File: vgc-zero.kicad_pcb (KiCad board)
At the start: 2 copper layers, 53 x 82 mm, 22 parts, among them J1 Conn_01x05_Pin, J2 Conn_01x05_Pin, J3 Conn_01x05_Pin, J4 Conn_01x02_Pin, SW1 SW_Push, SW10 SW_Push, SW11 SW_SPDT, SW2 SW_Push, SW3 SW_Push, SW4 SW_Push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

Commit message: pcb done
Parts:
- removed J4: Conn_01x02_Pin, Connector_PinHeader_1.00mm:PinHeader_1x02_P1.00mm_Horizontal
- added ?: , , F.Cu at (77.5, 79.5)
- added ?: , , F.Cu at (77.5, 75.0)
- added ?: , , F.Cu at (72.5, 79.0)
- added ?: , , F.Cu at (75.5, 73.0)
- added ?: , , F.Cu at (79.0, 82.0)
- added ?: , , F.Cu at (82.5, 75.5)
- added ?: , , F.Cu at (79.5, 73.0)
- added ?: , , F.Cu at (75.5, 82.0)
- added ?: , , F.Cu at (72.5, 75.5)
- added ?: , , F.Cu at (82.5, 79.0)
- added ?: , , F.Cu at (75.5, 77.0)
- added ?: , , F.Cu at (79.5, 77.0)
- added H1: MountingHole_Pad, MountingHole:MountingHole_3.2mm_M3_Pad, F.Cu at (77.0, 90.5)
- added REF**: MountingHole_2.2mm_M2, MountingHole:MountingHole_2.2mm_M2, F.Cu at (100.5, 40.5)
- D1: footprint LED_THT:LED_D3.0mm -> LED_SMD:LED_1210_3225Metric_Pad1.42x2.65mm_HandSolder
- J1, J2, J3: value Conn_01x05_Pin -> Conn_01x06_Pin; footprint Connector_PinHeader_1.00mm:PinHeader_1x05_P1.00mm_Horizontal -> Connector_PinHeader_2.54mm:PinHeader_1x06_P2.54mm_Horizontal
- moved J3 17.5 mm to (53.6, 114.6)
- moved J1 7.14 mm to (70.2, 114.6)
- moved D1 5.52 mm to (99.0, 46.0), turned to 0 degrees
- moved J2 4.17 mm to (86.7, 114.6)
- moved CHARGER1 1.03 mm to (75.0, 54.8)
- moved LS1 1.00 mm to (79.3, 68.5)
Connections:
- DISP1 pad 2: /3V3 -> 3V3
- MCU1 pad 36: /3V3 -> 3V3
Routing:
- net 3V3: track 0.00 -> 149.8 mm, vias 0 -> 2
- net /3V3: track 109.9 -> 0.00 mm, vias 3 -> 0
- net Net-(MCU1-GPIO7): track 31.5 -> 43.7 mm
- net Net-(MCU1-GPIO6): track 30.0 -> 38.6 mm
- net Net-(MCU1-GPIO9): track 24.4 -> 32.8 mm
- net Net-(J3-Pin_5): track 61.0 -> 52.9 mm
- net Net-(MCU1-GPIO10): track 39.3 -> 47.3 mm
- net Net-(MCU1-GPIO2): track 14.6 -> 22.6 mm
- net Net-(MCU1-GPIO5): track 37.2 -> 45.2 mm
- net Net-(MCU1-GPIO4): track 28.5 -> 36.5 mm
- net Net-(MCU1-GPIO3): track 39.3 -> 47.3 mm
- net Net-(MCU1-GPIO8): track 46.5 -> 54.5 mm
- net Net-(MCU1-GPIO11): track 11.0 -> 19.0 mm
- net Net-(J2-Pin_4): track 61.2 -> 53.5 mm
- net Net-(J2-Pin_5): track 59.2 -> 51.4 mm
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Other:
- board size 53 x 82 mm -> 53 x 87.5 mm
- board text added: "330Ω"

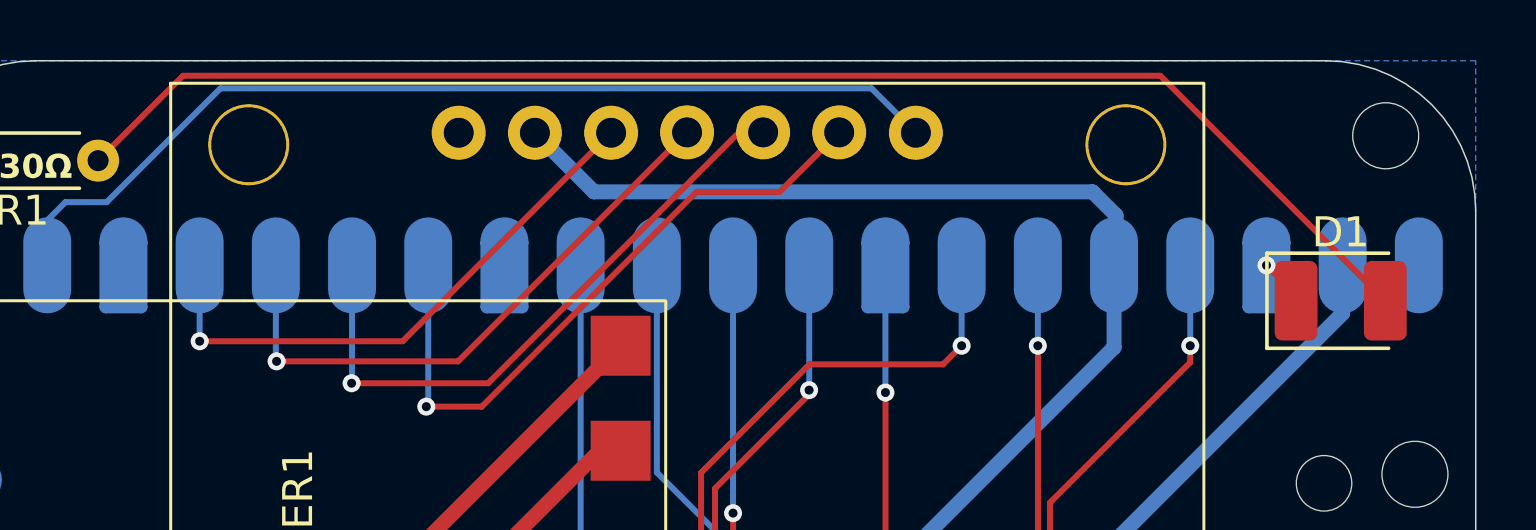
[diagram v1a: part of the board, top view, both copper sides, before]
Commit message: move via off the pad
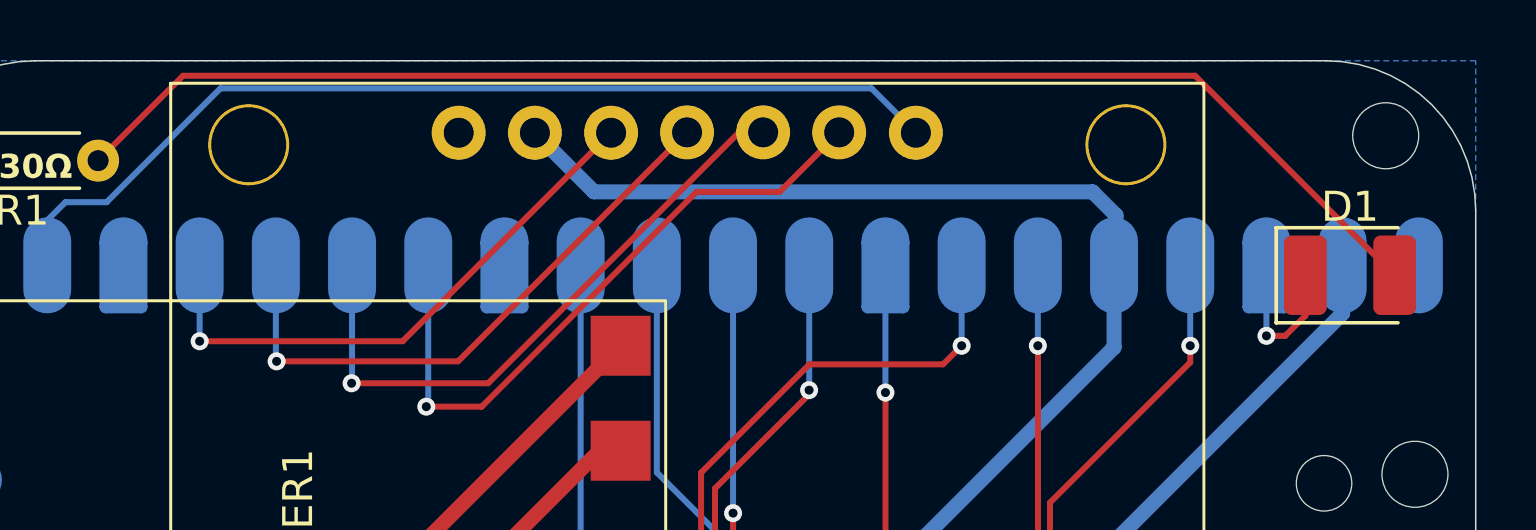
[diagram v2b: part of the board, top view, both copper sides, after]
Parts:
- moved D1 0.90 mm to (99.3, 45.1)
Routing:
- net /GND: track 16.8 -> 20.7 mm
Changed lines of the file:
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@@
 	(footprint "LED_SMD:LED_1210_3225Metric_Pad1.42x2.65mm_HandSolder"
 		(layer "F.Cu")
-		(at 99 46)
+		(at 99.31 45.15)
 		(descr "LED SMD 1210 (3225 Metric), square (rectangular) end terminal, IPC-7351 nominal, (Body size source: http://www.tortai-tech.com/upload/download/2011102023233369053.pdf), generated with kicad-footprint-generator")
 		(tags "LED handsolder")
@@
 	)
 	(segment
-		(start 97.5125 45.8075)
-		(end 96.525 44.82)
+		(start 97.15 47.17)
+		(end 97.8225 46.4975)
 		(width 0.2)
 		(layer "F.Cu")
@@
 	)
 	(segment
+		(start 97.8225 46.4975)
+		(end 97.8225 45.15)
+		(width 0.2)
+		(layer "F.Cu")
+		(net 3)
+	)
+	(segment
+		(start 96.525 47.17)
+		(end 97.15 47.17)
+		(width 0.2)
+		(layer "F.Cu")
+		(net 3)
+	)
+	(segment
 		(start 97.5125 46)
 		(end 97.5125 45.8075)
@@
 	)
 	(via
-		(at 96.525 44.82)
+		(at 96.525 47.17)
 		(size 0.6)
 		(drill 0.3)
@@
 	)
 	(segment
+		(start 96.525 47.17)
+		(end 96.525 44.82)
+		(width 0.2)
+		(layer "B.Cu")
+		(net 3)
+	)
+	(segment
 		(start 71.125 64.2)
 		(end 71.125 62.375)
@@
 	)
 	(segment
-		(start 100.4875 46)
-		(end 92.9875 38.5)
+		(start 100.7975 45.15)
+		(end 94.1475 38.5)
 		(width 0.2)
 		(layer "F.Cu")
@@
 	)
 	(segment
-		(start 92.9875 38.5)
+		(start 94.1475 38.5)
 		(end 60.41 38.5)
 		(width 0.2)

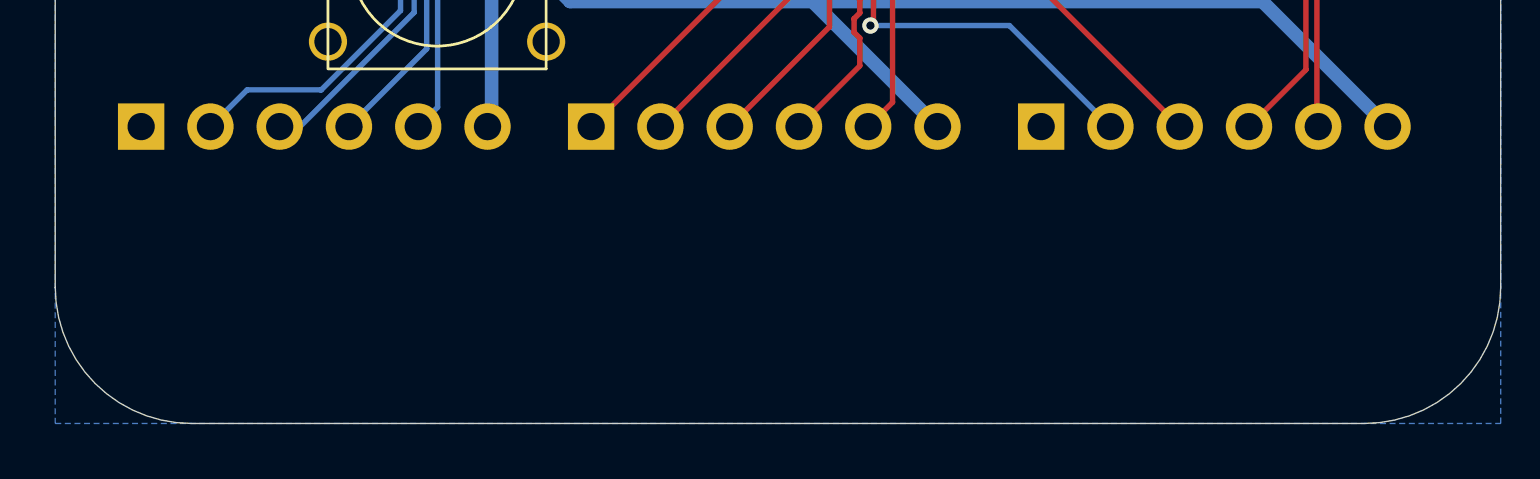
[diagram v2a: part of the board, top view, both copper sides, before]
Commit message: add markings
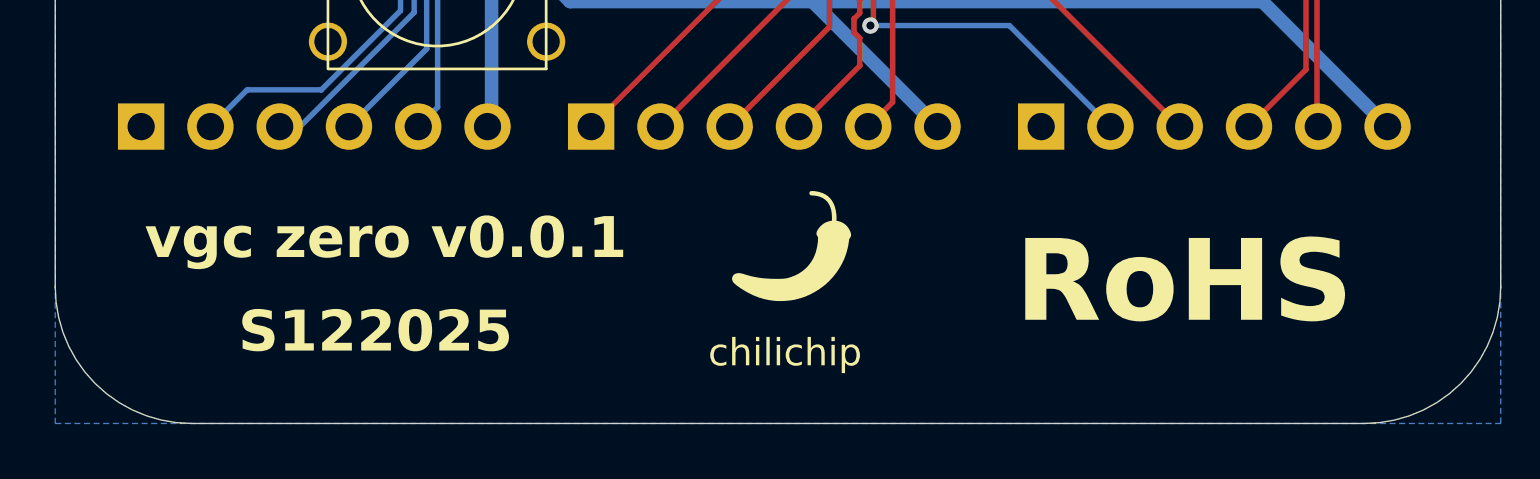
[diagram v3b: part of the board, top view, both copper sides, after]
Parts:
- added G***: LOGO, LOGO, F.Cu at (77.5, 119.1)
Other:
- board text added: "RoHS"
- board text added: "S122025"
- board text added: "chilichip"
- board text added: "vgc zero v0.0.1"

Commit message: final touches
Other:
- board text added: "vgc zero v0.0.2"
- board text removed: "vgc zero v0.0.1"
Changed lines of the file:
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@@
 	)
 	(paper "A4")
+	(title_block
+		(title "vgc zero")
+		(rev "v0.0.2")
+		(comment 4 "Author: Kacper Akdag-Ochnik")
+	)
 	(layers
 		(0 "F.Cu" signal)
@@
 		(tenting front back)
 		(pcbplotparams
-			(layerselection 0x00000000_00000000_55555555_5755f5ff)
+			(layerselection 0x00000000_00000000_55555555_575555ff)
 			(plot_on_all_layers_selection 0x00000000_00000000_00000000_00000000)
 			(disableapertmacros no)
@@
 			(usegerberattributes yes)
 			(usegerberadvancedattributes yes)
-			(creategerberjobfile yes)
+			(creategerberjobfile no)
 			(dashed_line_dash_ratio 12.000000)
 			(dashed_line_gap_ratio 3.000000)
@@
 			(outputformat 1)
 			(mirror no)
-			(drillshape 1)
+			(drillshape 0)
 			(scaleselection 1)
-			(outputdirectory "")
+			(outputdirectory "gerbers/")
 		)
 	)
@@
 		(layer "Edge.Cuts")
 	)
-	(gr_text "vgc zero v0.0.1"
+	(gr_text "vgc zero v0.0.2"
 		(at 53.78 119.58 0)
 		(layer "F.SilkS")
@@
 		)
 	)
+	(dimension
+		(type orthogonal)
+		(layer "F.SilkS")
+		(pts
+			(xy 103.5 120.5) (xy 50.5 120.5)
+		)
+		(height 8.55)
+		(orientation 0)
+		(format
+			(prefix "")
+			(suffix "")
+			(units 3)
+			(units_format 0)
+			(precision 4)
+			(suppress_zeroes yes)
+		)
+		(style
+			(thickness 0.1)
+			(arrow_length 1.27)
+			(text_position_mode 0)
+			(arrow_direction outward)
+			(extension_height 0.58642)
+			(extension_offset 0.5)
+			(keep_text_aligned yes)
+		)
+		(gr_text "53"
+			(at 77 127.95 0)
+			(layer "F.SilkS")
+			(effects
+				(font
+					(size 1 1)
+					(thickness 0.1)
+				)
+			)
+		)
+	)
+	(dimension
+		(type orthogonal)
+		(layer "F.SilkS")
+		(pts
+			(xy 98.5 38) (xy 98.5 125.5)
+		)
+		(height 8.97)
+		(orientation 1)
+		(format
+			(prefix "")
+			(suffix "")
+			(units 3)
+			(units_format 0)
+			(precision 4)
+			(suppress_zeroes yes)
+		)
+		(style
+			(thickness 0.1)
+			(arrow_length 1.27)
+			(text_position_mode 0)
+			(arrow_direction outward)
+			(extension_height 0.58642)
+			(extension_offset 0.5)
+			(keep_text_aligned yes)
+		)
+		(gr_text "87.5"
+			(at 106.37 81.75 90)
+			(layer "F.SilkS")
+			(effects
+				(font
+					(size 1 1)
+					(thickness 0.1)
+				)
+			)
+		)
+	)

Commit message: bump all the way to 1.0.0
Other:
- board text removed: "330Ω"
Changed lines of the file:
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@@
 	(title_block
 		(title "vgc zero")
-		(rev "v0.0.2")
+		(rev "v1.0.0")
+		(comment 3 "Company: chilichip")
 		(comment 4 "Author: Kacper Akdag-Ochnik")
 	)
@@
 				(bold yes)
 			)
-			(justify left bottom)
-		)
-	)
-	(gr_text "330Ω"
-		(at 53.5 42 0)
-		(layer "F.SilkS")
-		(effects
-			(font
-				(size 0.8 0.8)
-				(thickness 0.1)
-				(bold yes)
-			)

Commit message: minor fixes
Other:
- board text added: "vgc zero v1.0.1"
- board text removed: "vgc zero v0.0.2"
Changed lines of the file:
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@@
 	(title_block
 		(title "vgc zero")
-		(rev "v1.0.0")
+		(rev "v1.0.1")
 		(comment 3 "Company: chilichip")
 		(comment 4 "Author: Kacper Akdag-Ochnik")
@@
 		(at 69.6 40.4)
 		(property "Reference" "DISP1"
-			(at 7.62 17.85 0)
+			(at 22.08 37.36 0)
 			(unlocked yes)
 			(layer "F.SilkS")
@@
 		(layer "Edge.Cuts")
 	)
-	(gr_text "vgc zero v0.0.2"
+	(gr_text "vgc zero v1.0.1"
 		(at 53.78 119.58 0)
 		(layer "F.SilkS")

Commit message: update to 1.1.0
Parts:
- removed ? (x12): , 
- removed BT1: LIPO-BATTERY, Connector_JST:JST_PH_S2B-PH-K_1x02_P2.00mm_Horizontal
- removed CHARGER1: TP4056_CHARGER, vgc-zero-footprints:Tp4056_Charger
- removed REF**: MountingHole_2.2mm_M2, MountingHole:MountingHole_2.2mm_M2
- added H2: MountingHole_Pad, MountingHole:MountingHole_2.2mm_M2_Pad, F.Cu at (99.2, 44.0)
- added H3: MountingHole_Pad, MountingHole:MountingHole_2.2mm_M2_Pad, F.Cu at (59.8, 76.0)
- added H4: MountingHole_Pad, MountingHole:MountingHole_2.2mm_M2_Pad, F.Cu at (99.2, 76.0)
- added H5: MountingHole_Pad, MountingHole:MountingHole_2.2mm_M2_Pad, F.Cu at (59.8, 111.8)
- added H6: MountingHole_Pad, MountingHole:MountingHole_2.2mm_M2_Pad, F.Cu at (99.2, 111.8)
- DISP1: footprint vgc-zero-footprints:SSD1351_OLED_128x128 -> Connector_JST:JST_PH_S7B-PH-K_1x07_P2.00mm_Horizontal; moved to B.Cu
- H1: footprint MountingHole:MountingHole_3.2mm_M3_Pad -> MountingHole:MountingHole_2.2mm_M2_Pad
- LS1: footprint Connector_Wire:SolderWire-0.1sqmm_1x02_P3.6mm_D0.4mm_OD1mm -> Buzzer_Beeper:Buzzer_12x9.5RM7.6
- MCU1: footprint Module:RaspberryPi_Pico_SMD_HandSolder -> Module:RaspberryPi_Pico_Common_THT
- SW1, SW10, SW2, SW3, SW4, SW5, SW6, SW7, SW8, SW9: footprint vgc-zero-footprints:SW_PUSH_RUBBER_8mm -> Button_Switch_THT:SW_PUSH_6mm_H5mm
- moved H1 49.6 mm to (59.8, 44.0)
- moved J3 35.9 mm to (89.4, 117.5)
- moved DISP1 26.0 mm to (65.0, 66.0), turned to 90 degrees
- moved LS1 18.5 mm to (97.3, 64.0), turned to 90 degrees
- moved MCU1 18.5 mm to (88.4, 39.6), turned to 180 degrees
- moved SW10 14.8 mm to (62.5, 84.8), turned to 180 degrees
- moved J2 13.8 mm to (73.2, 117.5)
- moved J1 13.6 mm to (56.9, 117.5)
- moved SW2 12.4 mm to (103.0, 99.0), turned to -90 degrees
- moved SW1 12.2 mm to (103.0, 84.8), turned to 180 degrees
- moved SW4 10.3 mm to (93.5, 103.5), turned to -90 degrees
- moved SW11 9.88 mm to (57.2, 93.5)
- moved SW3 9.76 mm to (98.2, 89.0), turned to -90 degrees
- moved SW6 8.80 mm to (77.5, 98.4), turned to -90 degrees
- moved R1 7.83 mm to (60.2, 39.7)
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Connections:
- MCU1 pad 39: /VCC -> unconnected-(MCU1-VSYS-Pad39)
- SW11 pad 1: /VCC -> /GND
- SW11 pad 2: Net-(CHARGER1-OUT+) -> Net-(J2-Pin_3)
- SW11 pad 3: unconnected-(SW11-C-Pad3) -> 3V3
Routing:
- net /VCC: track 69.3 -> 0.00 mm, vias 1 -> 0
- net Net-(MCU1-GPIO16): track 3.84 -> 60.1 mm
- net Net-(CHARGER1-OUT+): track 45.5 -> 0.00 mm
- net Net-(J2-Pin_4): track 53.5 -> 94.5 mm, vias 1 -> 0
- net Net-(MCU1-GPIO11): track 19.0 -> 51.2 mm
- net Net-(J2-Pin_3): track 80.9 -> 112.4 mm, vias 1 -> 0
- net Net-(J3-Pin_2): track 59.0 -> 31.1 mm
- net Net-(J2-Pin_5): track 51.4 -> 79.2 mm, vias 1 -> 0
- net Net-(BT1--): track 27.0 -> 0.00 mm
- net Net-(BT1-+): track 24.2 -> 0.00 mm
- net Net-(J2-Pin_2): track 79.5 -> 56.2 mm, vias 2 -> 0
- net Net-(J3-Pin_3): track 56.1 -> 34.7 mm
- net Net-(MCU1-GPIO2): track 22.6 -> 42.9 mm
- net Net-(MCU1-GPIO9): track 32.8 -> 50.4 mm
- net Net-(J1-Pin_3): track 78.8 -> 61.3 mm, vias 1 -> 0
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- added copper zone on F.Cu, net /GND
- removed copper zone on B.Cu, net /GND
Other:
- board size 53 x 87.5 mm -> 50 x 90 mm
- board text added: "A"
- board text added: "B"
- board text added: "S012026"
- board text added: "X"
- board text added: "Y"
- board text added: "vgc zero v1.1.0"
- board text added: "≣"
- board text added: "⌂"
- board text added: "△"
- board text removed: "S122025"
- board text removed: "vgc zero v1.0.1"

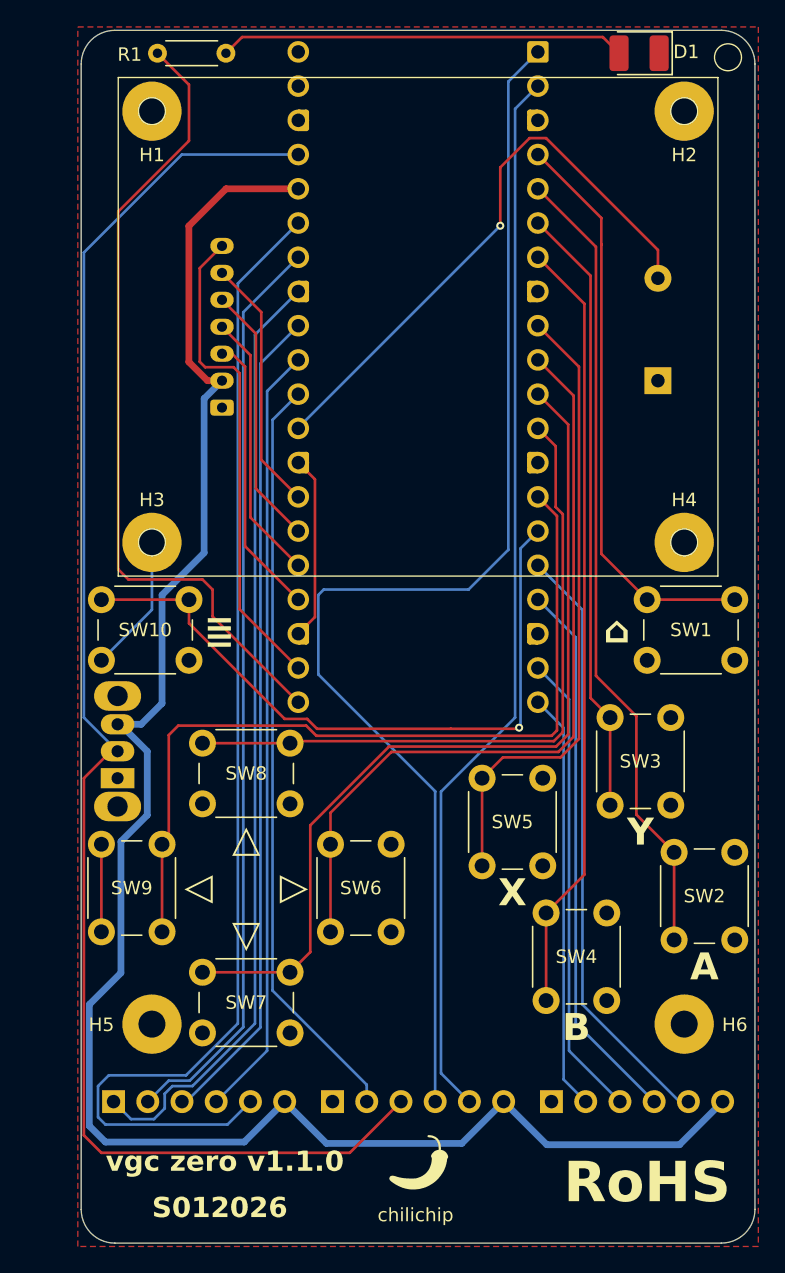
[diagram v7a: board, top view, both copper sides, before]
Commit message: adjust display pins
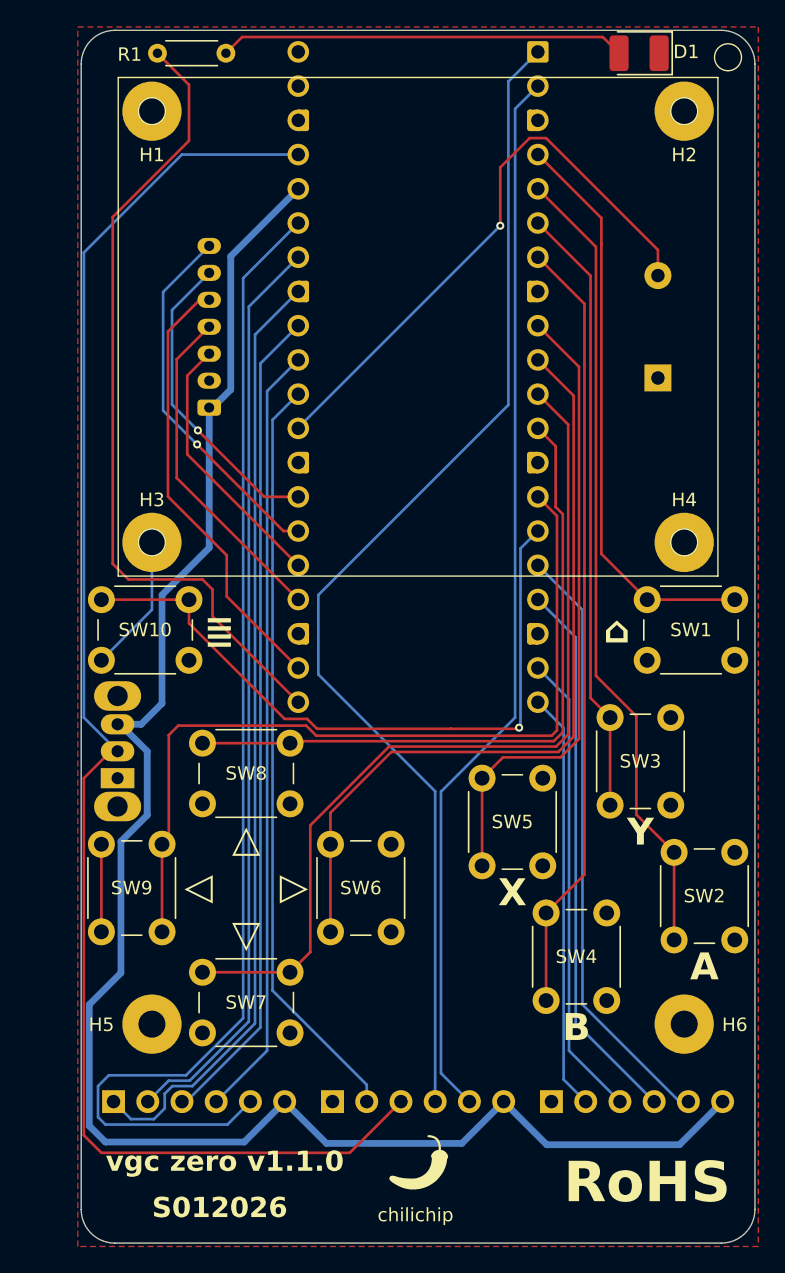
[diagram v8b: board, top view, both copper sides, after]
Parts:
- removed DISP1: SSD1351_OLED_128x128, Connector_JST:JST_PH_S7B-PH-K_1x07_P2.00mm_Horizontal
- added OLED1: DISP1, Connector_JST:JST_PH_S7B-PH-K_1x07_P2.00mm_Horizontal, B.Cu at (64.0, 66.0)
- moved LS1 0.20 mm to (97.3, 63.8)
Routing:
- net /GND: track 30.5 -> 16.8 mm
- net Net-(MCU1-GPIO20): track 19.5 -> 27.4 mm, vias 0 -> 1
- net Net-(J2-Pin_4): track 94.5 -> 88.2 mm
- net 3V3: track 138.7 -> 133.0 mm
- net Net-(MCU1-GPIO21): track 19.0 -> 23.1 mm, vias 0 -> 1
- net Net-(MCU1-GPIO18): track 21.0 -> 25.0 mm
- net Net-(MCU1-GPIO17): track 36.3 -> 33.0 mm
